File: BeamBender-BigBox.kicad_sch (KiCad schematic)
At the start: 158 parts, among them CN1 A4000-CN621-36, CN2 A4000-CN622-54, J1 HDMI, J2 JTAG, J3 JTAG_Pogo, J4 EXT_BUTTONS, J5 XAUDIO, J6 SJ1-3535NG, SW1 MENU, SW2 UP, SW3 DOWN, U1 Colorlight-i5-v7.0, U2 TLV76133DCYR, U3 74LVC16244ADGG, U4 74LVC16244ADGG, U5 SII9022ACNU, U6 74LVC1G86, U7 AK5720VT, U8 AP2112K-1.2, U9 OPA1692, X1 Oscillator_3.2x2.5mm-27MHz, X2 Oscillator_5.0x3.2mm_24.576MHz

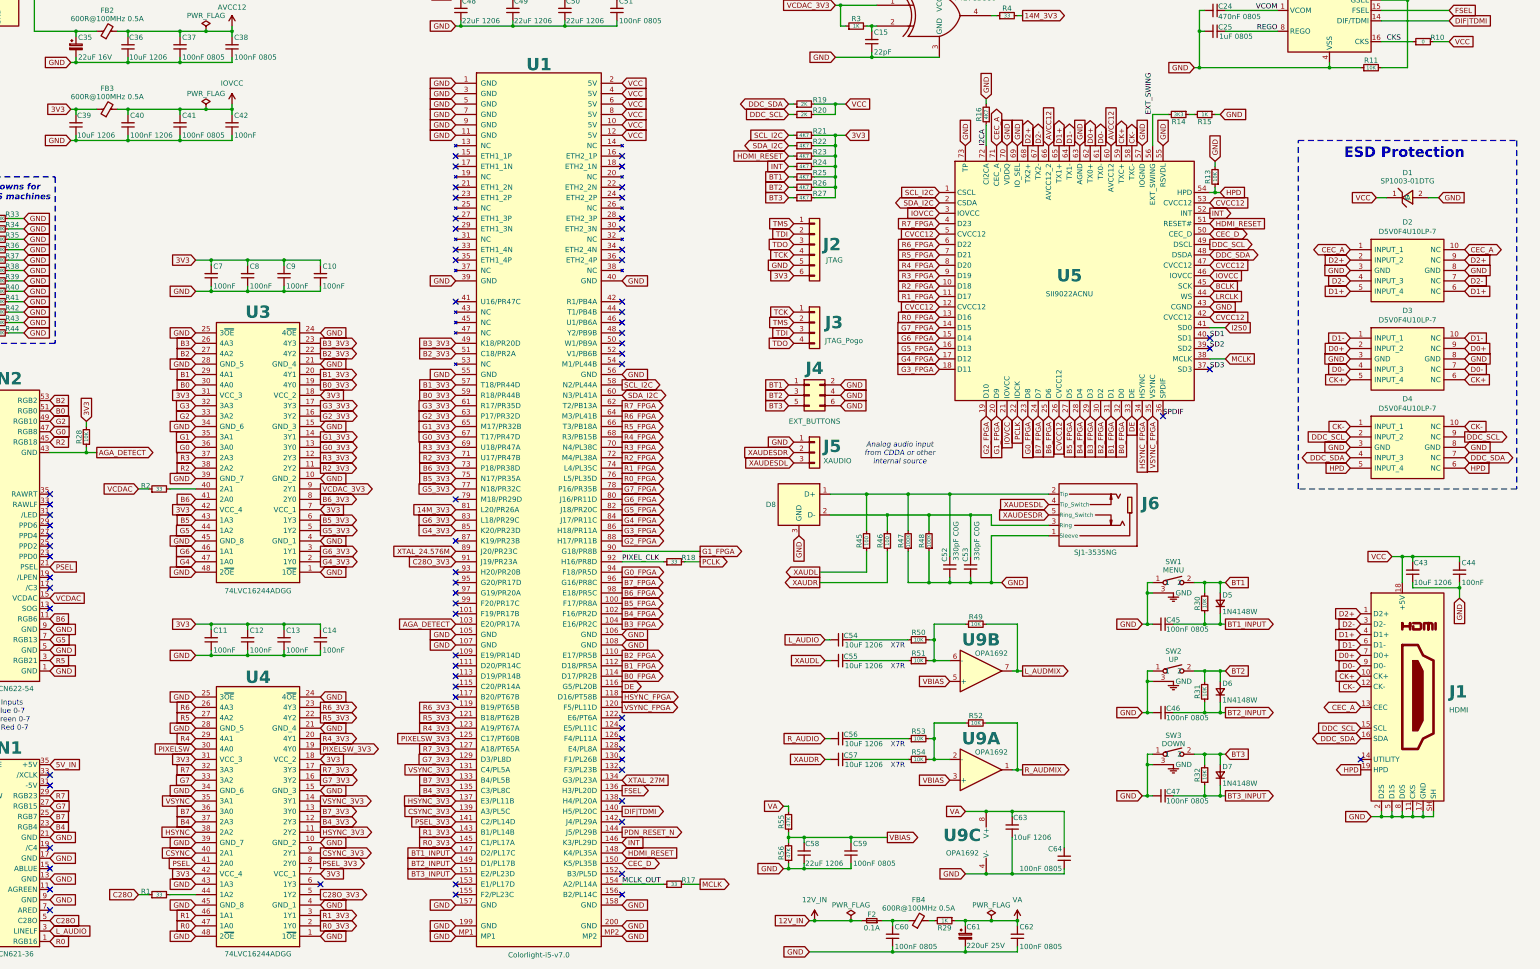
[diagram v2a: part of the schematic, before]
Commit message: Add HDMI back-feed protection
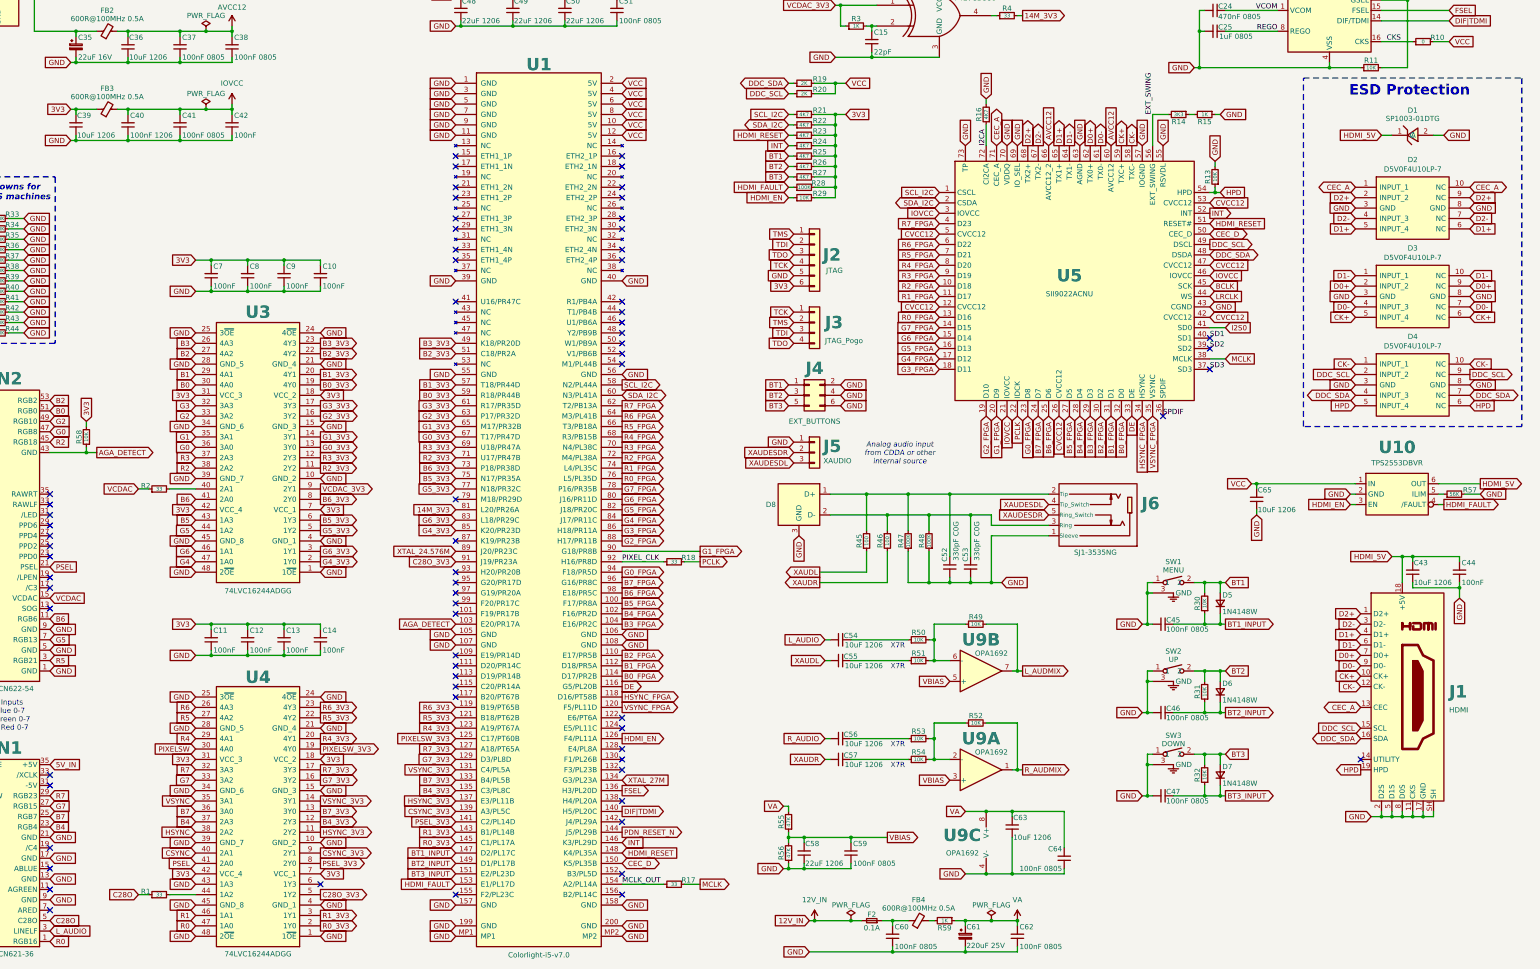
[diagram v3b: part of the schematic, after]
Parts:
- added C65: 10uF 1206, Capacitor_SMD:C_1206_3216Metric, symbol Device:C_Small
- added R28: 100K, Resistor_SMD:R_0603_1608Metric, symbol Device:R_Small
- added R29: 10K, Resistor_SMD:R_0603_1608Metric, symbol Device:R_Small
- added R57: 56K, Resistor_SMD:R_0603_1608Metric, symbol Device:R_Small
- added U10: TPS2553DBVR, Package_TO_SOT_SMD:SOT-23-6, symbol BeamBenderSymbols:TPS2553DBVR
- renumbered R28 to R58, R29 to R59
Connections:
- net 3V3: now also R28.2, R29.2
- net GND: now also C65.1, R57.2, U10.2 (GND)
- net VCC: now also C65.2, U10.1 (IN); no longer C43.2, C44.2, D1.1 (C), J1.18 (+5V)
- net HDMI_EN: now reaches U1.126 (F4/PL11A)
- net HDMI_EN: now also R29.1, U10.3 (EN)
- net HDMI_FAULT: now reaches U1.153 (E1/PL17D)
- net HDMI_FAULT: now also R28.1, U10.4 (/FAULT)
- new net: R57.1, U10.5 (ILIM)
- new net HDMI_5V: C43.2, C44.2, D1.1 (C), J1.18 (+5V), U10.6 (OUT)
- no-connect marks 83 -> 81
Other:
- moved on the sheet: D1, D2, D3, D4, J2, R19, R20, R21, R22, R23, R24, R25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

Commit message: Rev 0.3
Added test points for unused AV slot and FPGA pins
Added option to use Paula RAW audio
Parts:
- added R60: 0, Resistor_SMD:R_0603_1608Metric, symbol Device:R_Small
- added SJ1: LEFT, Jumper:SolderJumper-3_P1.3mm_Bridged12_RoundedPad1.0x1.5mm, symbol Jumper:SolderJumper_3_Bridged12
- added SJ2: RIGHT, Jumper:SolderJumper-3_P1.3mm_Bridged12_RoundedPad1.0x1.5mm, symbol Jumper:SolderJumper_3_Bridged12
- added TP1: TP_PPD7, TestPoint:TestPoint_Pad_D1.0mm, symbol Connector:TestPoint_Small
- added TP10: TP_PBUSY, TestPoint:TestPoint_Pad_D1.0mm, symbol Connector:TestPoint_Small
- added TP11: TP_PPOUT, TestPoint:TestPoint_Pad_D1.0mm, symbol Connector:TestPoint_Small
- added TP12: TP_LED, TestPoint:TestPoint_Pad_D1.0mm, symbol Connector:TestPoint_Small
- added TP13: TP_C3, TestPoint:TestPoint_Pad_D1.0mm, symbol Connector:TestPoint_Small
- added TP14: TP_SOG, TestPoint:TestPoint_Pad_D1.0mm, symbol Connector:TestPoint_Small
- added TP15: TP_TBASE, TestPoint:TestPoint_Pad_D1.0mm, symbol Connector:TestPoint_Small
- added TP16: TP_C1, TestPoint:TestPoint_Pad_D1.0mm, symbol Connector:TestPoint_Small
- added TP17: TP_XCLK, TestPoint:TestPoint_Pad_D1.0mm, symbol Connector:TestPoint_Small
- added TP18: TP_BLANK, TestPoint:TestPoint_Pad_D1.0mm, symbol Connector:TestPoint_Small
- added TP19: TP_C4, TestPoint:TestPoint_Pad_D1.0mm, symbol Connector:TestPoint_Small
- added TP2: TP_PPD6, TestPoint:TestPoint_Pad_D1.0mm, symbol Connector:TestPoint_Small
- added TP20: TP_XCLKEN, TestPoint:TestPoint_Pad_D1.0mm, symbol Connector:TestPoint_Small
- added TP21: TP_ABLUE, TestPoint:TestPoint_Pad_D1.0mm, symbol Connector:TestPoint_Small
- added TP22: TP_AGREEN, TestPoint:TestPoint_Pad_D1.0mm, symbol Connector:TestPoint_Small
- added TP23: TP_ARED, TestPoint:TestPoint_Pad_D1.0mm, symbol Connector:TestPoint_Small
- added TP24: TP_SPARE_IN5, TestPoint:TestPoint_Pad_D1.0mm, symbol Connector:TestPoint_Small
- added TP25: TP_SPARE_OUT3, TestPoint:TestPoint_Pad_D1.0mm, symbol Connector:TestPoint_Small
- added TP26: TP_FPGA41, TestPoint:TestPoint_Pad_D1.0mm, symbol Connector:TestPoint_Small
- added TP27: TP_FPGA79, TestPoint:TestPoint_Pad_D1.0mm, symbol Connector:TestPoint_Small
- added TP28: TP_FPGA87, TestPoint:TestPoint_Pad_D1.0mm, symbol Connector:TestPoint_Small
- added TP29: TP_FPGA93, TestPoint:TestPoint_Pad_D1.0mm, symbol Connector:TestPoint_Small
- added TP3: TP_PPD5, TestPoint:TestPoint_Pad_D1.0mm, symbol Connector:TestPoint_Small
- added TP30: TP_FPGA95, TestPoint:TestPoint_Pad_D1.0mm, symbol Connector:TestPoint_Small
- added TP31: TP_FPGA97, TestPoint:TestPoint_Pad_D1.0mm, symbol Connector:TestPoint_Small
- added TP32: TP_FPGA99, TestPoint:TestPoint_Pad_D1.0mm, symbol Connector:TestPoint_Small
- added TP33: TP_FPGA101, TestPoint:TestPoint_Pad_D1.0mm, symbol Connector:TestPoint_Small
- added TP34: TP_FPGA109, TestPoint:TestPoint_Pad_D1.0mm, symbol Connector:TestPoint_Small
- added TP35: TP_FPGA111, TestPoint:TestPoint_Pad_D1.0mm, symbol Connector:TestPoint_Small
- added TP36: TP_FPGA113, TestPoint:TestPoint_Pad_D1.0mm, symbol Connector:TestPoint_Small
- added TP37: TP_FPGA115, TestPoint:TestPoint_Pad_D1.0mm, symbol Connector:TestPoint_Small
- added TP38: TP_FPGA117, TestPoint:TestPoint_Pad_D1.0mm, symbol Connector:TestPoint_Small
- added TP39: TP_FPGA155, TestPoint:TestPoint_Pad_D1.0mm, symbol Connector:TestPoint_Small
- added TP4: TP_PPD4, TestPoint:TestPoint_Pad_D1.0mm, symbol Connector:TestPoint_Small
- added TP40: TP_FPGA42, TestPoint:TestPoint_Pad_D1.0mm, symbol Connector:TestPoint_Small
- added TP41: TP_FPGA44, TestPoint:TestPoint_Pad_D1.0mm, symbol Connector:TestPoint_Small
- added TP42: TP_FPGA46, TestPoint:TestPoint_Pad_D1.0mm, symbol Connector:TestPoint_Small
- added TP43: TP_FPGA48, TestPoint:TestPoint_Pad_D1.0mm, symbol Connector:TestPoint_Small
- added TP44: TP_FPGA50, TestPoint:TestPoint_Pad_D1.0mm, symbol Connector:TestPoint_Small
- added TP45: TP_FPGA52, TestPoint:TestPoint_Pad_D1.0mm, symbol Connector:TestPoint_Small
- added TP46: TP_FPGA54, TestPoint:TestPoint_Pad_D1.0mm, symbol Connector:TestPoint_Small
- added TP47: TP_FPGA122, TestPoint:TestPoint_Pad_D1.0mm, symbol Connector:TestPoint_Small
- added TP48: TP_FPGA124, TestPoint:TestPoint_Pad_D1.0mm, symbol Connector:TestPoint_Small
- added TP49: TP_FPGA128, TestPoint:TestPoint_Pad_D1.0mm, symbol Connector:TestPoint_Small
- added TP5: TP_PPD3, TestPoint:TestPoint_Pad_D1.0mm, symbol Connector:TestPoint_Small
- added TP50: TP_FPGA130, TestPoint:TestPoint_Pad_D1.0mm, symbol Connector:TestPoint_Small
- added TP51: TP_FPGA132, TestPoint:TestPoint_Pad_D1.0mm, symbol Connector:TestPoint_Small
- added TP52: TP_FPGA138, TestPoint:TestPoint_Pad_D1.0mm, symbol Connector:TestPoint_Small
- added TP53: TP_FPGA142, TestPoint:TestPoint_Pad_D1.0mm, symbol Connector:TestPoint_Small
- added TP54: TP_FPGA152, TestPoint:TestPoint_Pad_D1.0mm, symbol Connector:TestPoint_Small
- added TP55: TP_FPGA156, TestPoint:TestPoint_Pad_D1.0mm, symbol Connector:TestPoint_Small
- added TP6: TP_PPD2, TestPoint:TestPoint_Pad_D1.0mm, symbol Connector:TestPoint_Small
- added TP7: TP_PPD1, TestPoint:TestPoint_Pad_D1.0mm, symbol Connector:TestPoint_Small
- added TP8: TP_PPD0, TestPoint:TestPoint_Pad_D1.0mm, symbol Connector:TestPoint_Small
- added TP9: TP_PACK, TestPoint:TestPoint_Pad_D1.0mm, symbol Connector:TestPoint_Small
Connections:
- net GND: now also R60.2; no longer U4.43 (1A3)
- net L_AUDIO: now also SJ1.1 (A); no longer C54.1
- net R_AUDIO: now also SJ2.1 (A); no longer C56.1
- net #SOG: now reaches CN2.13 (SOG)
- net #SOG: now also TP14.1
- net #TBASE: now reaches CN2.14 (TBASE)
- net #TBASE: now also TP15.1
- net #PPOUT: now reaches CN2.16 (PPOUT)
- net #PPOUT: now also TP11.1
- net #C3: now reaches CN2.17 (/C3)
- net #C3: now also TP13.1
- net #PBUSY: now reaches CN2.18 (PBUSY)
- net #PBUSY: now also TP10.1
- net #PACK: now reaches CN2.20 (/PACK)
- net #PACK: now also TP9.1
- net #PPD0: now reaches CN2.23 (PPD0)
- net #PPD0: now also TP8.1
- net #PPD1: now reaches CN2.24 (PPD1)
- net #PPD1: now also TP7.1
- net #PPD2: now reaches CN2.25 (PPD2)
- net #PPD2: now also TP6.1
- net #PPD3: now reaches CN2.26 (PPD3)
- net #PPD3: now also TP5.1
- net #PPD4: now reaches CN2.27 (PPD4)
- net #PPD4: now also TP4.1
- net #PPD5: now reaches CN2.28 (PPD5)
- net #PPD5: now also TP3.1
- net #PPD6: now reaches CN2.29 (PPD6)
- net #PPD6: now also TP2.1
- net #PPD7: now reaches CN2.30 (PPD7)
- net #PPD7: now also TP1.1
- net #LED: now reaches CN2.31 (/LED)
- net #LED: now also TP12.1
- net RAWLF: now reaches CN2.33 (RAWLF)
- net RAWLF: now also SJ1.3 (B)
- net RAWRT: now reaches CN2.35 (RAWRT)
- net RAWRT: now also SJ2.3 (B)
- net SPARE_OUT3: now reaches U4.6 (1Y3)
- net SPARE_OUT3: now also TP25.1
- net #AGREEN: now reaches CN1.11 (AGREEN)
- net #AGREEN: now also TP22.1
- net #ABLUE: now reaches CN1.15 (ABLUE)
- net #ABLUE: now also TP21.1
- net #XCLKEN: now reaches CN1.16 (/XCLKEN)
- net #XCLKEN: now also TP20.1
- net #C4: now reaches CN1.19 (/C4)
- net #C4: now also TP19.1
- net #BLANK: now reaches CN1.28 (BLANK)
- net #BLANK: now also TP18.1
- net #XCLK: now reaches CN1.33 (/XCLK)
- net #XCLK: now also TP17.1
- net #C1: now reaches CN1.34 (/C1)
- net #C1: now also TP16.1
- net #ARED: now reaches CN1.7 (ARED)
- net #ARED: now also TP23.1
- net #FPGA101: now reaches U1.101 (F19/PR17B)
- net #FPGA101: now also TP33.1
- net #FPGA109: now reaches U1.109 (E19/PR14D)
- net #FPGA109: now also TP34.1
- net #FPGA111: now reaches U1.111 (D20/PR14C)
- net #FPGA111: now also TP35.1
- net #FPGA113: now reaches U1.113 (D19/PR14B)
- net #FPGA113: now also TP36.1
- net #FPGA115: now reaches U1.115 (C20/PR14A)
- net #FPGA115: now also TP37.1
- net #FPGA117: now reaches U1.117 (B20/PT67B)
- net #FPGA117: now also TP38.1
- net #FPGA122: now reaches U1.122 (E6/PT6A)
- net #FPGA122: now also TP47.1
- net #FPGA124: now reaches U1.124 (E5/PL11C)
- net #FPGA124: now also TP48.1
- net #FPGA128: now reaches U1.128 (E4/PL8A)
- net #FPGA128: now also TP49.1
- net #FPGA130: now reaches U1.130 (F1/PL26B)
- net #FPGA130: now also TP50.1
- net #FPGA132: now reaches U1.132 (F3/PL23B)
- net #FPGA132: now also TP51.1
- net #FPGA138: now reaches U1.138 (H4/PL20A)
- net #FPGA138: now also TP52.1
- net #FPGA142: now reaches U1.142 (J4/PL29A)
- net #FPGA142: now also TP53.1
- net #FPGA152: now reaches U1.152 (B3/PL5D)
- net #FPGA152: now also TP54.1
- net #FPGA155: now reaches U1.155 (F2/PL23C)
- net #FPGA155: now also TP39.1
- net #FPGA156: now reaches U1.156 (B2/PL14C)
- net #FPGA156: now also TP55.1
- net #FPGA41: now reaches U1.41 (U16/PR47C)
- net #FPGA41: now also TP26.1
- net #FPGA42: now reaches U1.42 (R1/PB4A)
- net #FPGA42: now also TP40.1
- net #FPGA44: now reaches U1.44 (T1/PB4B)
- net #FPGA44: now also TP41.1
- net #FPGA46: now reaches U1.46 (U1/PB6A)
- net #FPGA46: now also TP42.1
- net #FPGA48: now reaches U1.48 (Y2/PB9B)
- net #FPGA48: now also TP43.1
- net #FPGA50: now reaches U1.50 (W1/PB9A)
- net #FPGA50: now also TP44.1
- net #FPGA52: now reaches U1.52 (V1/PB6B)
- net #FPGA52: now also TP45.1
- net #FPGA54: now reaches U1.54 (M1/PL44B)
- net #FPGA54: now also TP46.1
- net #FPGA79: now reaches U1.79 (M18/PR29D)
- net #FPGA79: now also TP27.1
- net #FPGA87: now reaches U1.87 (K19/PR23B)
- net #FPGA87: now also TP28.1
- net #FPGA93: now reaches U1.93 (H20/PR20B)
- net #FPGA93: now also TP29.1
- net #FPGA95: now reaches U1.95 (G20/PR17D)
- net #FPGA95: now also TP30.1
- net #FPGA97: now reaches U1.97 (G19/PR20A)
- net #FPGA97: now also TP31.1
- net #FPGA99: now reaches U1.99 (F20/PR17C)
- net #FPGA99: now also TP32.1
- new net: C56.1, SJ2.2 (C)
- new net: C54.1, SJ1.2 (C)
- new net SPARE_IN5: R60.1, TP24.1, U4.43 (1A3)
- no-connect marks 81 -> 25
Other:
- note added: "Test Points for Unused Pins"
- moved on the sheet: C1, C10, C11, C12, C13, C14, C15, C16, C17, C18, C19, C2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

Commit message: Firmware 2026-10-30.03, BBLink 1.30, rev 0.3 production files and docs updates
Firmware (Firmware/: 2026-10-30.03 for the i9 and i5, standard and -c28, in place of 2026-10-28.04)
- Capture Clock on Display Info is steady: measured over 64 ms and shown to the nearest kHz, so it no longer flickers between two values.
- The input Frame Rate is timed against the card's own 27 MHz clock and holds steady (a PAL screen no longer flips between 49.91 and 49.92 Hz).
- The output frame rate is rounded like the input's: both read 50.38 Hz for a PAL screen on an NTSC-crystal machine with the -c28 firmware.
- Capture Width goes up to 800 and is shown in the screen's own pixels (up to 1360 on a Super-Hires screen); BB-800x600 on ECS shows all 800 columns.
- New defaults: Status Lines Hidden, Menu Position Bottom Right, Menu Background 50%.
- Settings record version 15 (since 2026-10-28.05): older records are not read, so back up with BBLink before updating from 2026-10-28.04 or earlier.
- The Amiga control link filters out short glitches on its lines.
- On-screen text in American spelling (Initializing, No RGB (gray), OSD Colors).

BBLink (BBLink/)
- bblink.lha: BBLink 1.30 (values in white on the live pages, as on the card), BBSurvey 1.12 (the 355-byte settings record), BBKeyCon, BBMode and BBProbe rebuilt for 2026-10-30.03. BBLag and BBScreen unchanged.
- README.md: the 2026-10-28.05 settings record, `[OSD Colors]` in backups (older `[OSD Colours]` files still load), values in white, examples for 1.30.
- Monitors/README.md: BB-800x600 on ECS shows all 800 columns. Monitors/bbmonitors.lha repacked; the drivers are unchanged.

Documentation
- Firmware/README.md: a new module's flash is unlocked through the card's JTAG header with `openFPGALoader -c ft232 --unprotect-flash` (one power cycle may be needed before the first write); the ecpdap and dev-board steps and the memory load (`-m`) are removed; sections reordered (adapter, software, unlock, write); the -c28 NTSC rate corrected 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
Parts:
- R12: now not fitted; now left out of the parts list
- R49, R52: value 10K -> 8K2; LCSC C25804 -> C25981; MPN 0603WAF1002T5E -> 0603WAF8201T5E
- R51, R54: value 10K -> 20K; LCSC C25804 -> C4184; MPN 0603WAF1002T5E -> 0603WAF2002T5E
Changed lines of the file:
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@@
 			)
 		)
-		(property "Value" "10K"
+		(property "Value" "20K"
 			(at 339.09 234.95 90)
 			(show_name no)
@@
 			)
 		)
-		(property "LCSC" "C25804"
+		(property "LCSC" "C4184"
 			(at 339.09 234.95 90)
 			(hide yes)
@@
 			)
 		)
-		(property "MPN" "0603WAF1002T5E"
+		(property "MPN" "0603WAF2002T5E"
 			(at 339.09 234.95 90)
 			(hide yes)
@@
 		(body_style 1)
 		(exclude_from_sim no)
-		(in_bom yes)
+		(in_bom no)
 		(on_board yes)
-		(in_pos_files yes)
-		(dnp no)
+		(in_pos_files no)
+		(dnp yes)
 		(property "Reference" "R12"
 			(at 449.58 26.162 90)
@@
 			)
 		)
-		(property "Value" "10K"
+		(property "Value" "8K2"
 			(at 353.06 201.93 90)
 			(show_name no)
@@
 			)
 		)
-		(property "LCSC" "C25804"
+		(property "LCSC" "C25981"
 			(at 353.06 201.93 90)
 			(hide yes)
@@
 			)
 		)
-		(property "MPN" "0603WAF1002T5E"
+		(property "MPN" "0603WAF8201T5E"
 			(at 353.06 201.93 90)
 			(hide yes)
@@
 			)
 		)
-		(property "Value" "10K"
+		(property "Value" "8K2"
 			(at 353.06 226.06 90)
 			(show_name no)
@@
 			)
 		)
-		(property "LCSC" "C25804"
+		(property "LCSC" "C25981"
 			(at 353.06 226.06 90)
 			(hide yes)
@@
 			)
 		)
-		(property "MPN" "0603WAF1002T5E"
+		(property "MPN" "0603WAF8201T5E"
 			(at 353.06 226.06 90)
 			(hide yes)
@@
 			)
 		)
-		(property "Value" "10K"
+		(property "Value" "20K"
 			(at 339.09 210.82 90)
 			(show_name no)
@@
 			)
 		)
-		(property "LCSC" "C25804"
+		(property "LCSC" "C4184"
 			(at 339.09 210.82 90)
 			(hide yes)
@@
 			)
 		)
-		(property "MPN" "0603WAF1002T5E"
+		(property "MPN" "0603WAF2002T5E"
 			(at 339.09 210.82 90)
 			(hide yes)
